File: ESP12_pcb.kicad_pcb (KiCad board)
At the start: 2 copper layers, 36.8 x 36.8 mm, 31 parts, among them CON1 ZX62D1-B-5PA(30), J1 CONN_01X02, J2 CONN_01X02_FEMALE, Q1 IRLML9301TRPBF, Q2 IRLML9301TRPBF, U1 LD1117DT33TR, U2 TPS61090

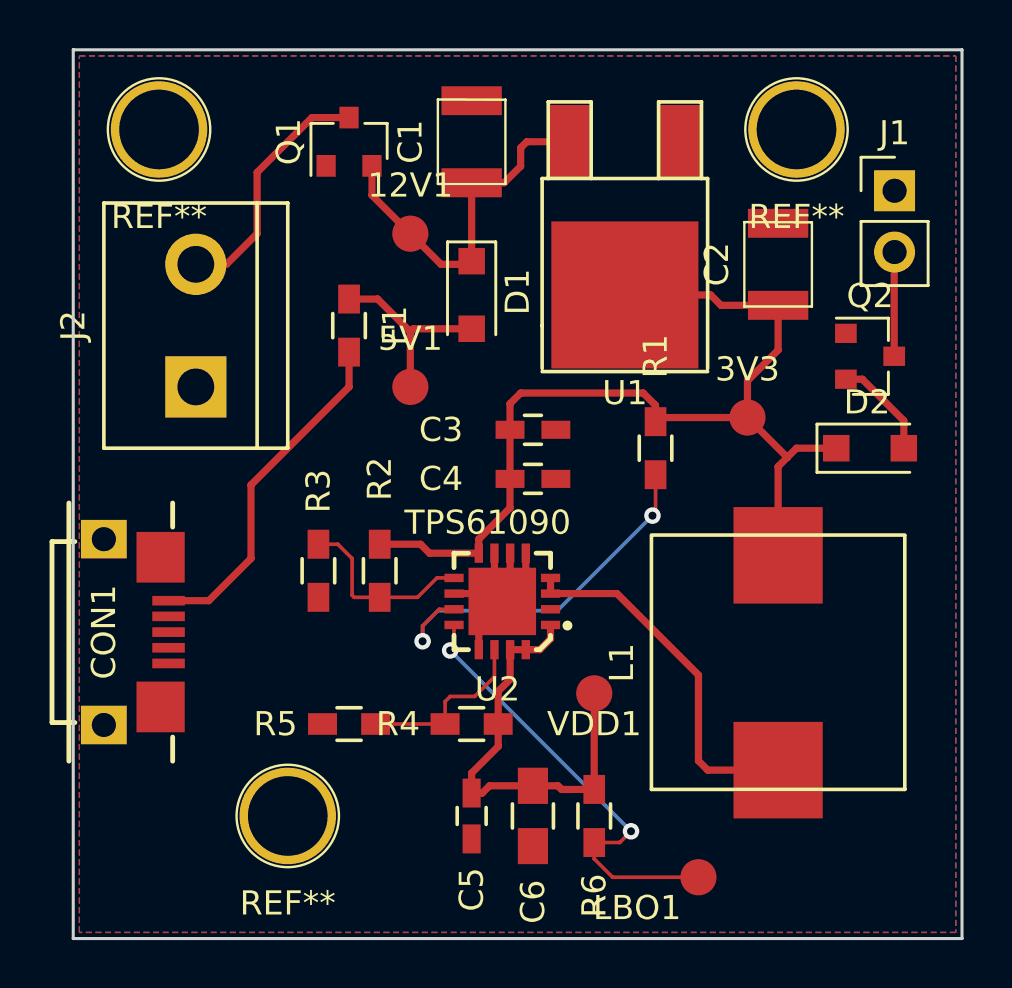
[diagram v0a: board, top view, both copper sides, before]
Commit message: Modified Top silk screen
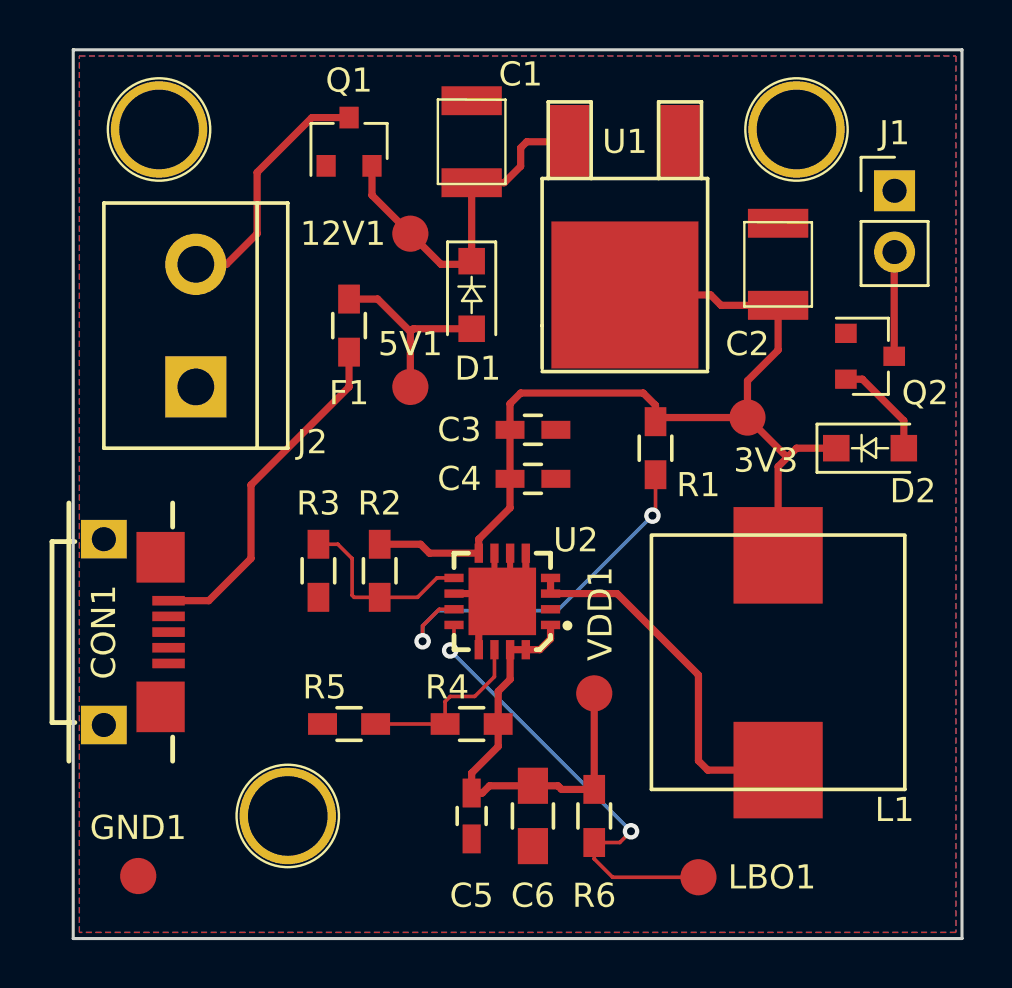
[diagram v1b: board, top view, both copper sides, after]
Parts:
- added GND1: TEST, Measurement_Points:Measurement_Point_Round-SMD-Pad_Small, F.Cu at (101.8, 114.2)
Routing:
- net GND: track 11.2 -> 13.7 mm

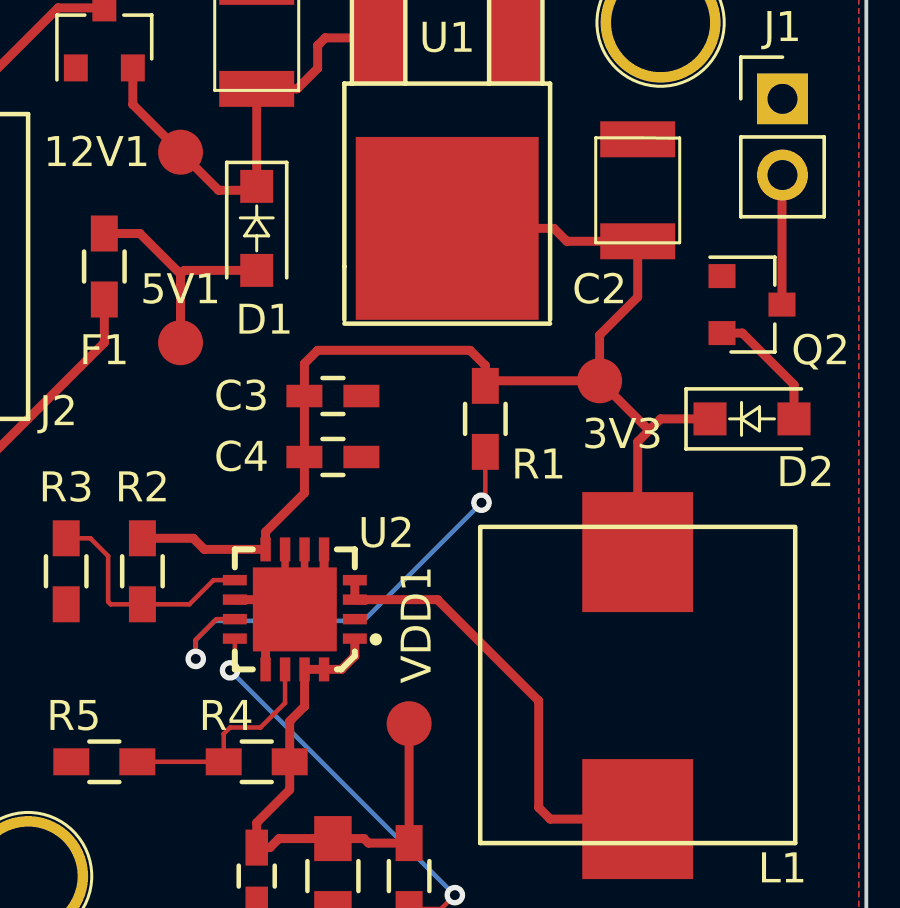
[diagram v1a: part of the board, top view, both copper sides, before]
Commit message: Changed one connection for AP2112k
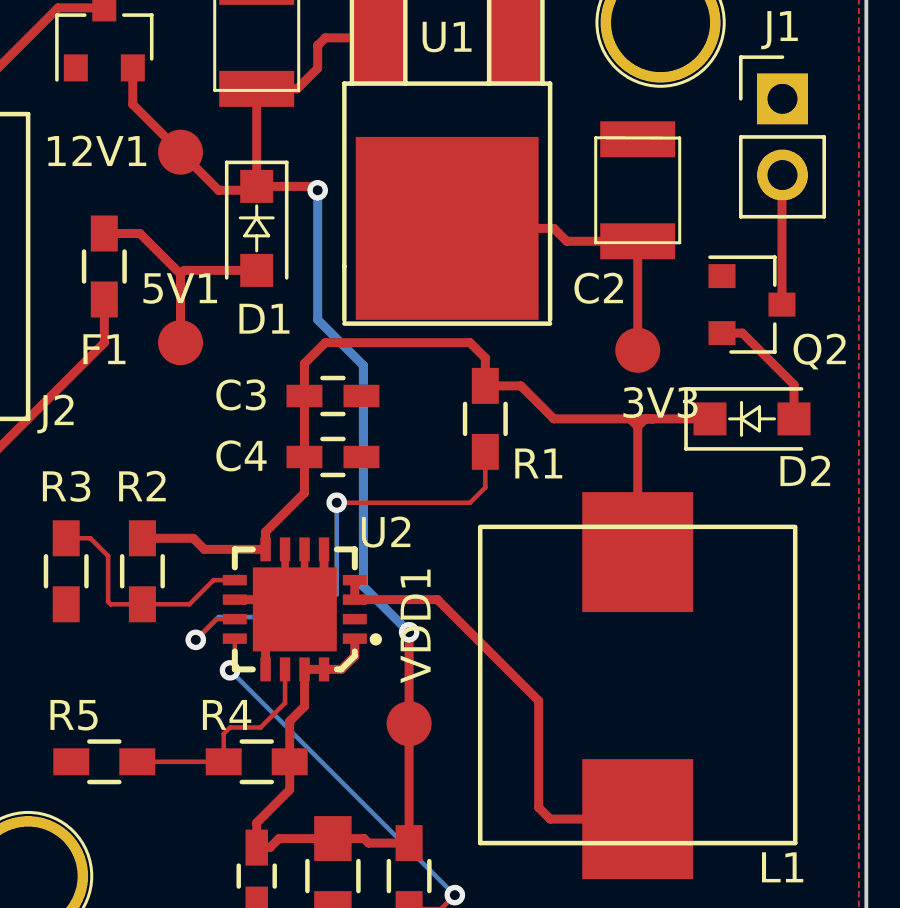
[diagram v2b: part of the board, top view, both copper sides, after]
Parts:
- moved 3V3 1.63 mm to (128.3, 94.2)
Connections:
- C1 pad 1: +12V -> VDD
- C3 pad 1: +3V3 -> Net-(C3-Pad1)
- C4 pad 1: +3V3 -> Net-(C3-Pad1)
- D1 pad 1: +12V -> VDD
- D2 pad 1: +3V3 -> Net-(C3-Pad1)
- L1 pad 1: +3V3 -> Net-(C3-Pad1)
- R1 pad 1: +3V3 -> Net-(C3-Pad1)
- R2 pad 1: +3V3 -> Net-(C3-Pad1)
- U1 pad 3: +12V -> VDD
- U2 pad 8: +3V3 -> Net-(C3-Pad1)
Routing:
- net +3V3: track 42.8 -> 10.2 mm
- net Net-(C3-Pad1): track 0.00 -> 31.8 mm
- net VDD: track 18.3 -> 50.0 mm, vias 0 -> 2
- net +12V: track 15.9 -> 5.26 mm

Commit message: Version V0.1 sended to fabrication
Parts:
- removed 12V1, 3V3, 5V1, GND1, LBO1, VDD1: TEST, Measurement_Points:Measurement_Point_Round-SMD-Pad_Small
- removed CON1: ZX62D1-B-5PA(30), papayagroup:USB-micro-B_Hirose
- removed D1, D2: MBR120VLSFT3G, Diodes_SMD:D_SOD-123F
- removed F1: 0603L100SLYR, Resistors_SMD:R_0603_HandSoldering
- removed J2: CONN_01X02_FEMALE, Connectors:bornier2
- removed Q1: IRLML9301TRPBF, TO_SOT_Packages_SMD:SOT-23
- removed the REF** at (108.0, 111.8)
- removed the REF** at (129.0, 83.3)
- removed the REF** at (102.6, 83.3)
- removed U2: TPS61090, papayagroup:QFN65P400X400X100-17N
- added J3: Conn_02x04_Odd_Even, Pin_Headers:Pin_Header_Straight_2x04_Pitch2.54mm, B.Cu at (45.8, 86.3)
- added R10: 10k, Resistors_SMD:R_0603_HandSoldering, F.Cu at (52.7, 82.9)
- added R11: 10k, Resistors_SMD:R_0603_HandSoldering, F.Cu at (50.0, 82.9)
- added R12: 10k, Resistors_SMD:R_0603_HandSoldering, F.Cu at (51.4, 83.0)
- added R7: 0, Resistors_SMD:R_0603_HandSoldering, F.Cu at (44.3, 71.2)
- added R8: 220k, Resistors_SMD:R_0603_HandSoldering, F.Cu at (44.3, 74.3)
- added R9: 1M, Resistors_SMD:R_0603_HandSoldering, F.Cu at (48.7, 82.9)
- added REF**: via0305, papayagroup:via0305, F.Cu at (42.9, 87.7)
- added REF**: via0305, papayagroup:via0305, F.Cu at (43.3, 66.2)
- added REF**: via0305, papayagroup:via0305, F.Cu at (44.2, 66.2)
- added REF**: via0305, papayagroup:via0305, F.Cu at (56.5, 66.7)
- added REF**: via0305, papayagroup:via0305, F.Cu at (56.5, 67.5)
- added REF**: via0305, papayagroup:via0305, F.Cu at (56.5, 68.4)
- added REF**: via0305, papayagroup:via0305, F.Cu at (50.3, 71.8)
- added REF**: via0305, papayagroup:via0305, F.Cu at (49.1, 71.8)
- added REF**: via0305, papayagroup:via0305, F.Cu at (50.3, 68.3)
- added REF**: via0305, papayagroup:via0305, F.Cu at (49.1, 68.3)
- added REF**: via0305, papayagroup:via0305, F.Cu at (54.0, 85.0)
- added REF**: via0305, papayagroup:via0305, F.Cu at (56.5, 87.7)
- added REF**: via0305, papayagroup:via0305, F.Cu at (56.5, 88.6)
- added REF**: via0305, papayagroup:via0305, F.Cu at (56.5, 89.5)
- added REF**: via0305, papayagroup:via0305, F.Cu at (55.5, 89.8)
- added REF**: via0305, papayagroup:via0305, F.Cu at (43.8, 89.8)
- added REF**: via0305, papayagroup:via0305, F.Cu at (42.9, 88.6)
- added REF**: via0305, papayagroup:via0305, F.Cu at (42.9, 89.5)
- added REF**: via0305, papayagroup:via0305, F.Cu at (45.1, 66.2)
- added SW1: SW_Push, papayagroup:button_4pin, B.Cu at (49.7, 78.0)
- added TP1: bat, Measurement_Points:Measurement_Point_Round-SMD-Pad_Small, F.Cu at (49.7, 78.0)
- added TP2: vdd, Measurement_Points:Measurement_Point_Round-SMD-Pad_Small, F.Cu at (43.5, 83.7)
- added TP3: LBO, Measurement_Points:Measurement_Point_Round-SMD-Pad_Small, F.Cu at (45.8, 83.8)
- C1: footprint papayagroup:C_3528 -> Capacitors_SMD:C_0603_HandSoldering; moved to B.Cu
- C2: value 10uF -> 100nF; footprint papayagroup:C_3528 -> Capacitors_SMD:C_0603_HandSoldering
- C6: footprint Capacitors_SMD:C_0805_HandSoldering -> papayagroup:smd_5_5.4
- L1: footprint papayagroup:L_bourns -> papayagroup:smd_L_4532
- R4: value 1,87M -> 2M
- R5: value 200k -> 2M
- R6: value 1M -> 12M
- U1: value LD1117DT33TR -> TPS61030PWR; footprint TO_SOT_Packages_SMD:TO-252-2Lead -> papayagroup:R-PDSO-16; moved to B.Cu
- moved R6 85.7 mm to (44.3, 72.8), turned to 180 degrees
- moved L1 83.1 mm to (53.9, 68.3), turned to 180 degrees
- moved R4 81.7 mm to (44.3, 68.0)
- moved Q2 80.8 mm to (52.5, 78.9), turned to 180 degrees
- moved C5 79.9 mm to (44.4, 75.7), turned to 180 degrees
- moved C6 79.6 mm to (45.5, 79.2)
- moved J1 77.9 mm to (55.5, 80.2), turned to 180 degrees
- moved R5 76.5 mm to (44.3, 69.5), turned to 0 degrees
- moved R1 76.3 mm to (50.4, 73.5), turned to 180 degrees
- moved C2 74.5 mm to (54.0, 82.8)
- moved U1 73.5 mm to (49.7, 70.0), turned to 270 degrees
- moved C4 67.3 mm to (55.1, 74.2)
- moved C3 66.2 mm to (55.1, 75.4)
- moved R2 64.1 mm to (55.1, 71.5), turned to 0 degrees
- moved C1 62.8 mm to (53.0, 78.0), turned to 90 degrees
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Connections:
- C1 pad 1: VDD -> /RST
- C2 pad 1: +3V3 -> VDD
- C3 pad 1: Net-(C3-Pad1) -> +BATT
- C4 pad 1: Net-(C3-Pad1) -> +BATT
- L1 pad 1: Net-(C3-Pad1) -> +BATT
- R1 pad 1: Net-(C3-Pad1) -> +BATT
- R2 pad 1: Net-(C3-Pad1) -> +BATT
- R5 pad 2: GND -> Net-(R5-Pad2)
- R6 pad 1: VDD -> Net-(R5-Pad2)
- R6 pad 2: /LBO -> /FB
- U1 pad 1: GND -> Net-(L1-Pad2)
- U1 pad 2: +3V3 -> Net-(L1-Pad2)
- U1 pad 3: VDD -> GND
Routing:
- net Net-(C3-Pad1): track 31.8 -> 0.00 mm
- net /RST: track 0.00 -> 19.6 mm, vias 0 -> 1
- net VDD: track 50.0 -> 32.9 mm, vias 2 -> 1
- net +BATT: track 4.25 -> 19.5 mm, vias 0 -> 2
- net Net-(CON1-Pad1): track 14.4 -> 0.00 mm
- net GND: track 13.7 -> 0.00 mm
- net /TPEN: track 16.3 -> 3.79 mm, vias 2 -> 1
- net Net-(L1-Pad2): track 15.2 -> 4.41 mm, vias 0 -> 1
- net Net-(J2-Pad2): track 10.4 -> 0.00 mm
- net +3V3: track 10.2 -> 0.00 mm
- net +5V: track 7.98 -> 0.00 mm
- net /FB: track 0.00 -> 6.29 mm, vias 0 -> 1
- net Net-(R4-Pad2): track 7.40 -> 1.60 mm
- net /CH_PD: track 0.00 -> 5.55 mm
- net +12V: track 5.26 -> 0.00 mm
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- added copper zone on B.Cu, net Net-(L1-Pad2)
- added copper zone on B.Cu, net VDD
- added copper zone on F.Cu, net VDD
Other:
- board size 36.8 x 36.8 mm -> 15 x 25 mm
- board text added: "10"
- board text added: "11"
- board text added: "12"
- board text added: "C1"
- board text added: "C2"
- board text added: "C3"
- board text added: "C4"
- board text added: "C5"
- board text added: "C6"
- board text added: "GND"
- board text added: "IoT Button V0.1 Darkomen"
- board text added: "R1"
- board text added: "R2"
- board text added: "R3"
- board text added: "R4"
- board text added: "R5"
- board text added: "R6"
- board text added: "R7"
- board text added: "R8"
- board text added: "R9"
- board text added: "VCC"
